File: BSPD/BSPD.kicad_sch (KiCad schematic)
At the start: 27 parts, among them J1 350826-1, J2 440054-2, Q3 PMOS, U1 LM339DR, U2 R-78E5.0-0.5, U3 SN74LVC1G08DBVR, U4 SN74LVC3G14DCUR, U5 NE555DR, U6 SN74LVC1G08DBVR, U7 SN74HC32DR

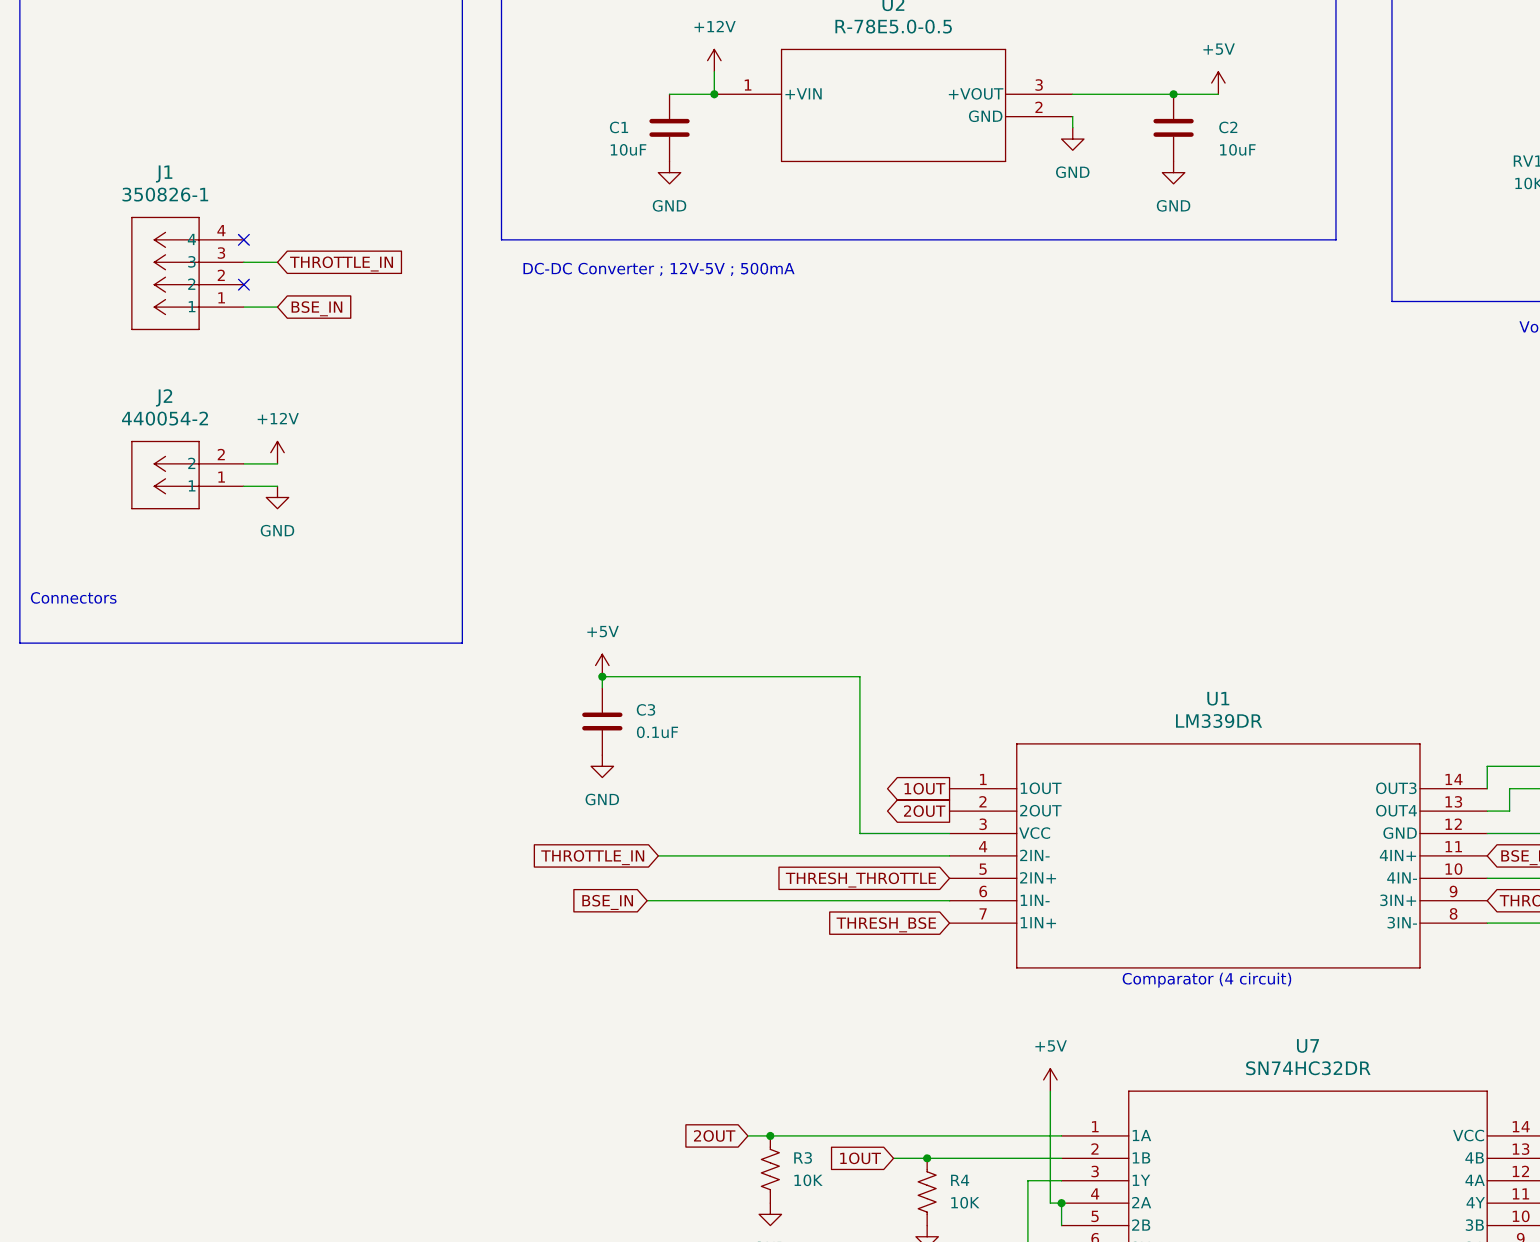
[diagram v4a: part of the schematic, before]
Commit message: Updating footprints
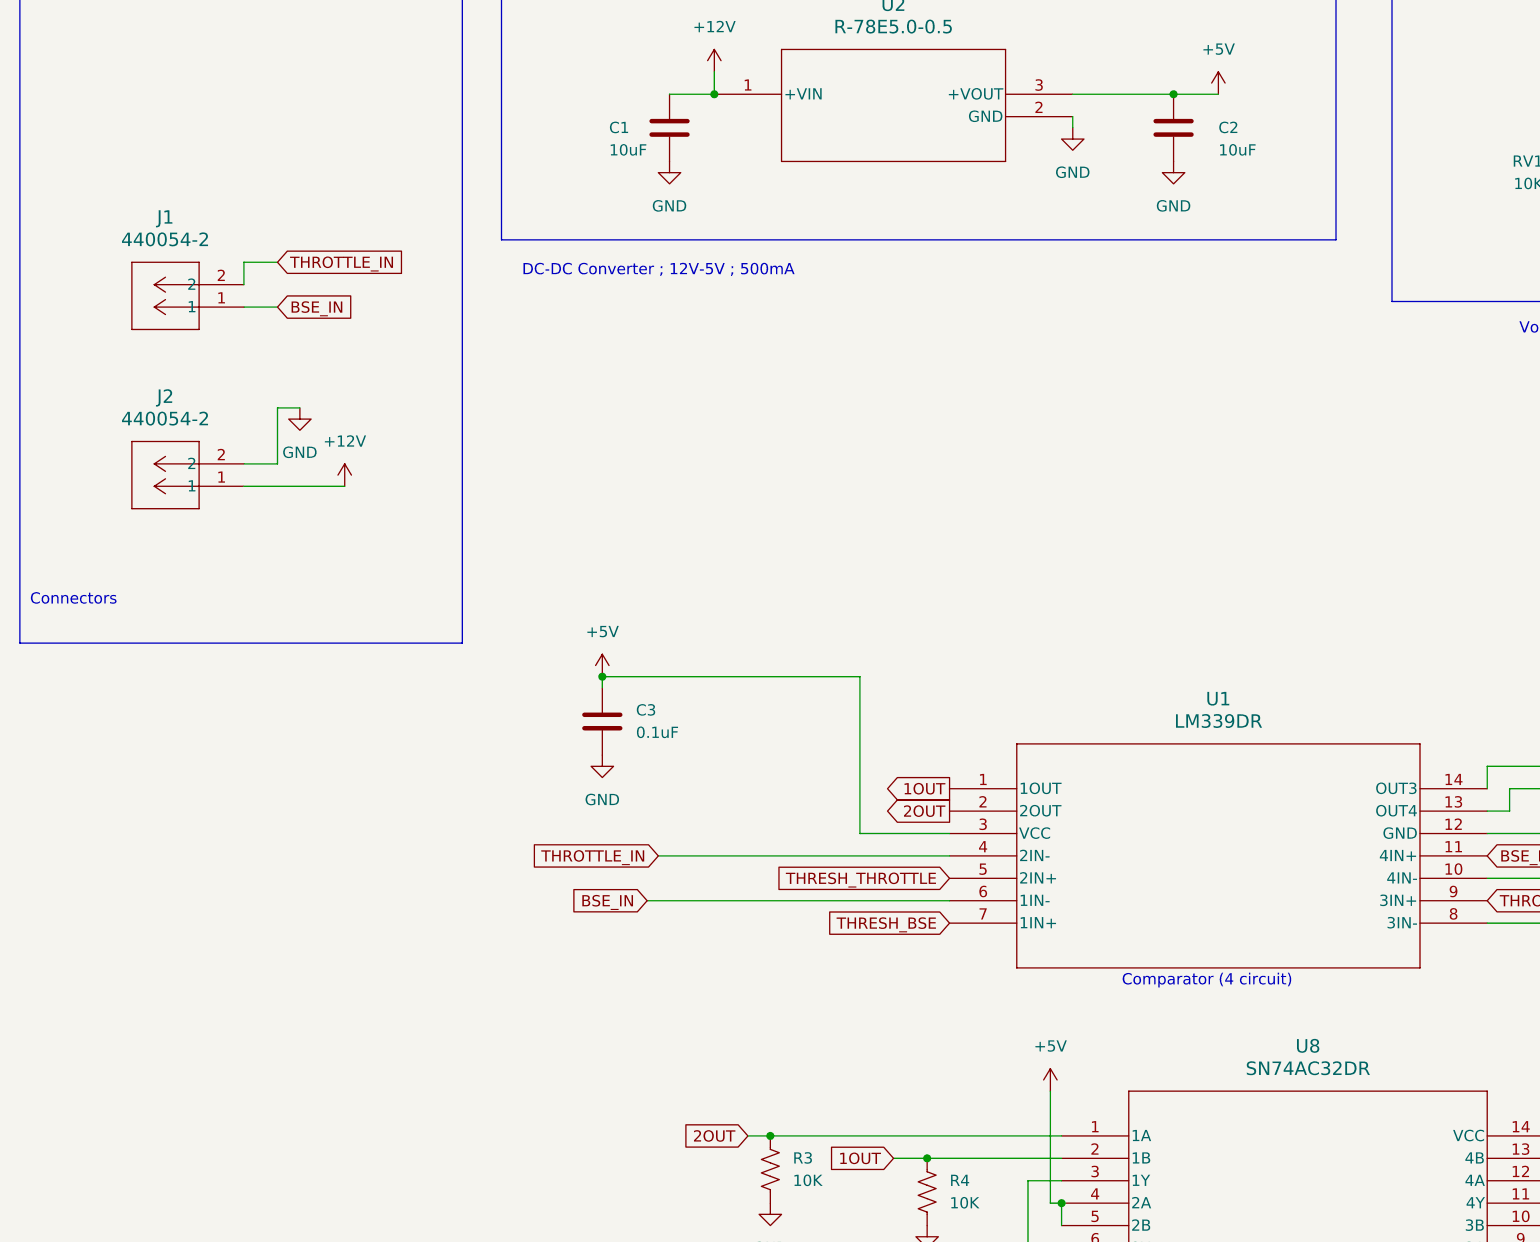
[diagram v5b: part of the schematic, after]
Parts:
- removed J1: 350826-1, 350826-1:CONN_350826-1_TYC, symbol 350826-1:350826-1
- removed U7: SN74HC32DR, SN74AC32DR:D14, symbol SN74AC32DR:SN74AC32DR
- added J1: 440054-2, 440054_2:CONN2_440054-2_TYC, symbol 440054_2:440054-2
- added U8: SN74AC32DR, D14, symbol SN74AC32DR:SN74AC32DR
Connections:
- net +12V: now also J2.1; no longer J2.2
- net 1OUT: now also U8.2 (1B)
- net 2OUT: now also U8.1 (1A)
- net BSE_IN: now also J1.1
- net BSPD_OUT: now also U8.8 (3Y)
- net GND: now also J2.2, U8.7 (GND); no longer J2.1
- net THROTTLE_IN: now also J1.2
- net at C7.1, R2.2: now also U8.10 (3B)
- net at C6.1: now also U8.12 (4A), U8.13 (4B), U8.14 (VCC)
- net at U4.1 (1A), U6.1 (A): now also U8.3 (1Y)
- net at U6.4 (Y): now also U8.9 (3A)
- new net: U8.4 (2A), U8.5 (2B)
- no-connect marks 2 -> 0

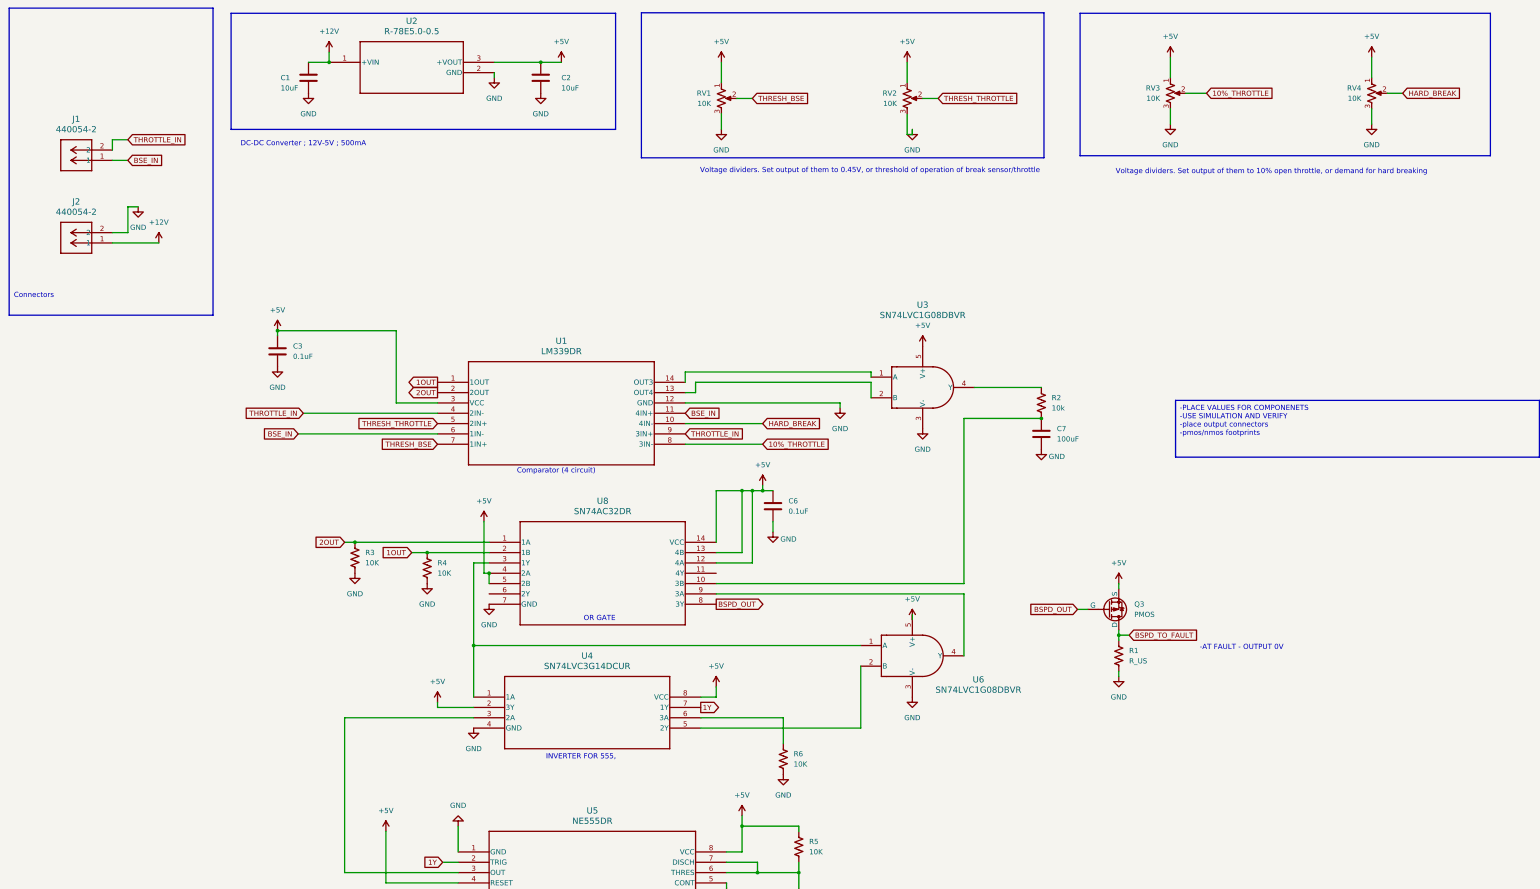
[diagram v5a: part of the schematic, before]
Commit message: Connector changes, layout, edge cuts, constraints. Need advice on output PMOS
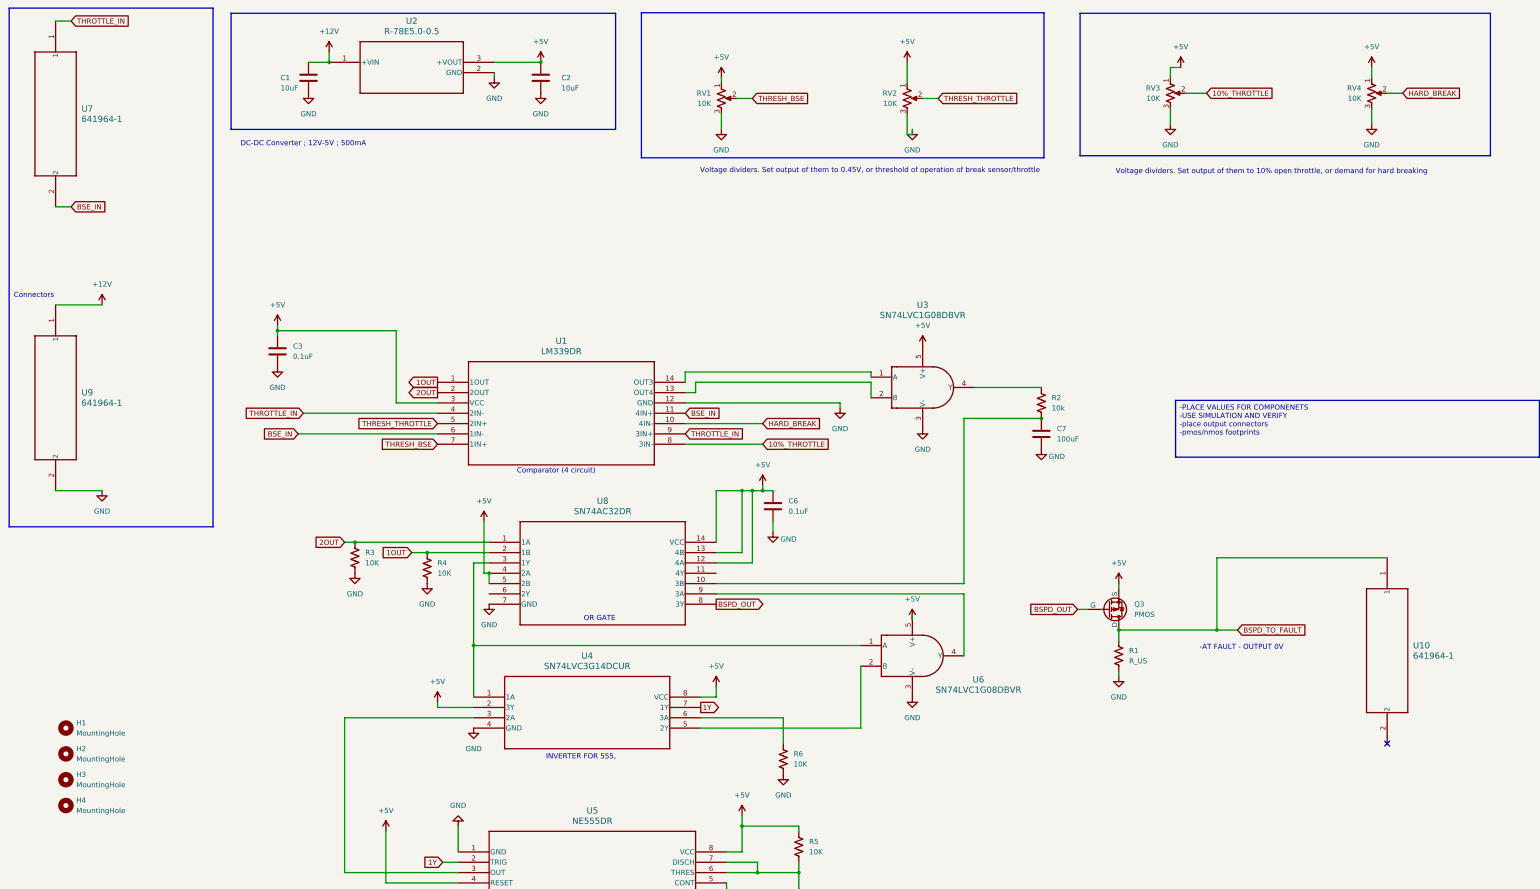
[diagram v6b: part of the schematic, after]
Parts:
- removed J1, J2: 440054-2, 440054_2:CONN2_440054-2_TYC, symbol 440054_2:440054-2
- added H1, H2, H3, H4: MountingHole, MountingHole:MountingHole_2.2mm_M2, symbol Mechanical:MountingHole
- added U10, U7, U9: 641964-1, 641964-1:641964-1_TYC, symbol 641964-1:641964-1
- Q3: footprint (none) -> Package_TO_SOT_SMD:SOT-23
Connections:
- net +12V: now also U9.1
- net +5V: now also C2.1, C3.1, RV1.1, RV2.1, RV3.1, RV4.1, U1.3 (VCC), U2.3 (+VOUT)
- net BSE_IN: now also U7.2
- net BSPD_TO_FAULT: now also U10.1
- net GND: now also U9.2
- net THROTTLE_IN: now also U7.1
- no-connect marks 0 -> 1

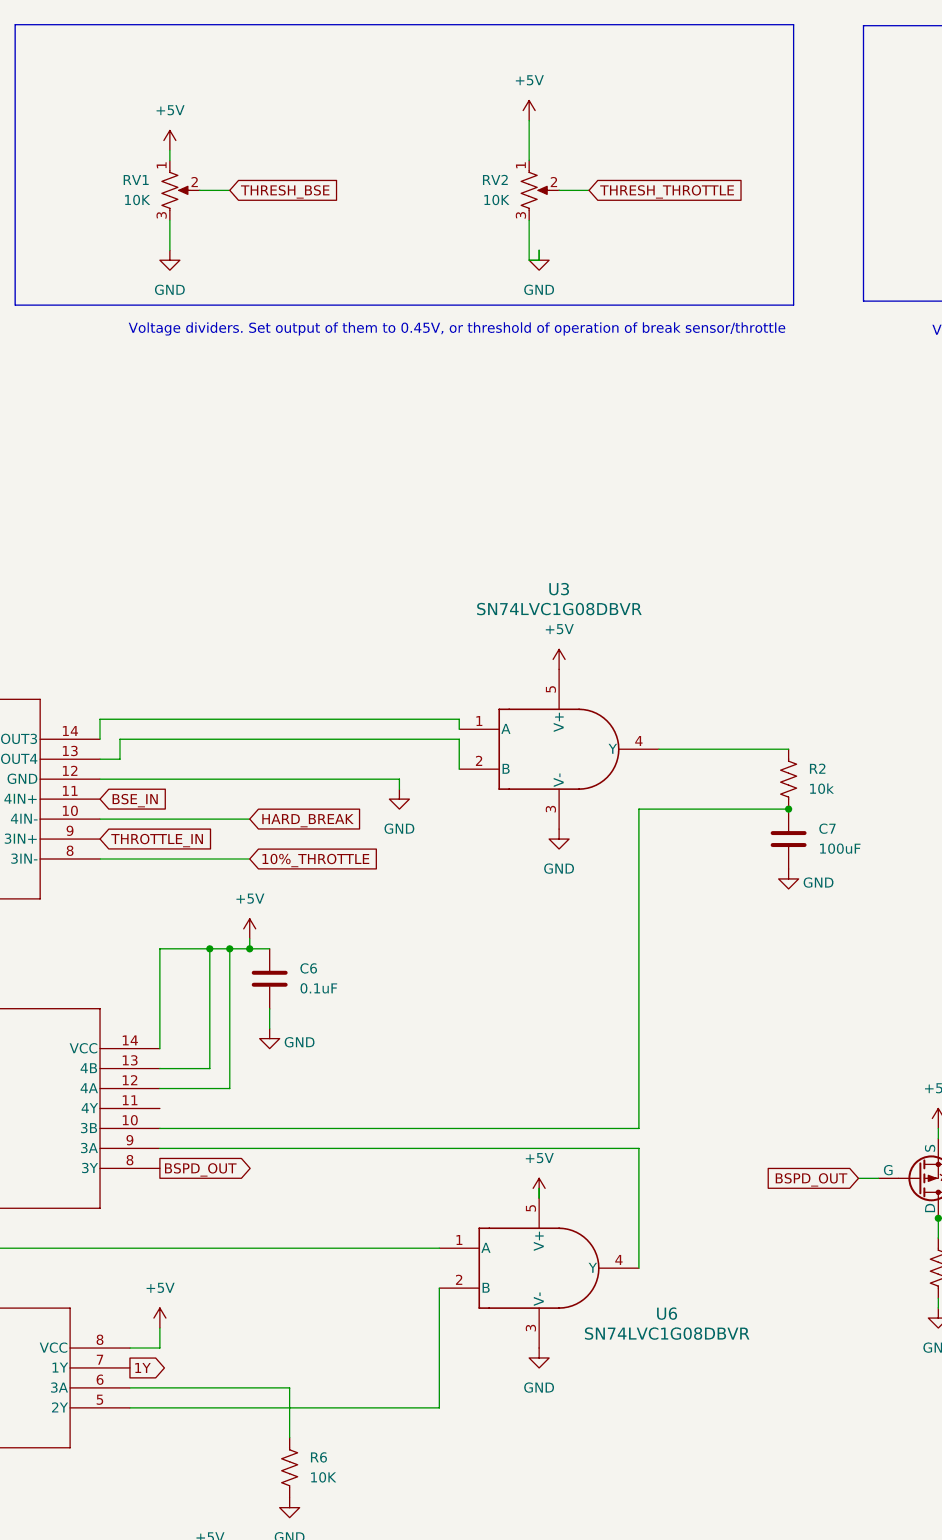
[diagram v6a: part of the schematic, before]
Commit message: Bypass caps bspd
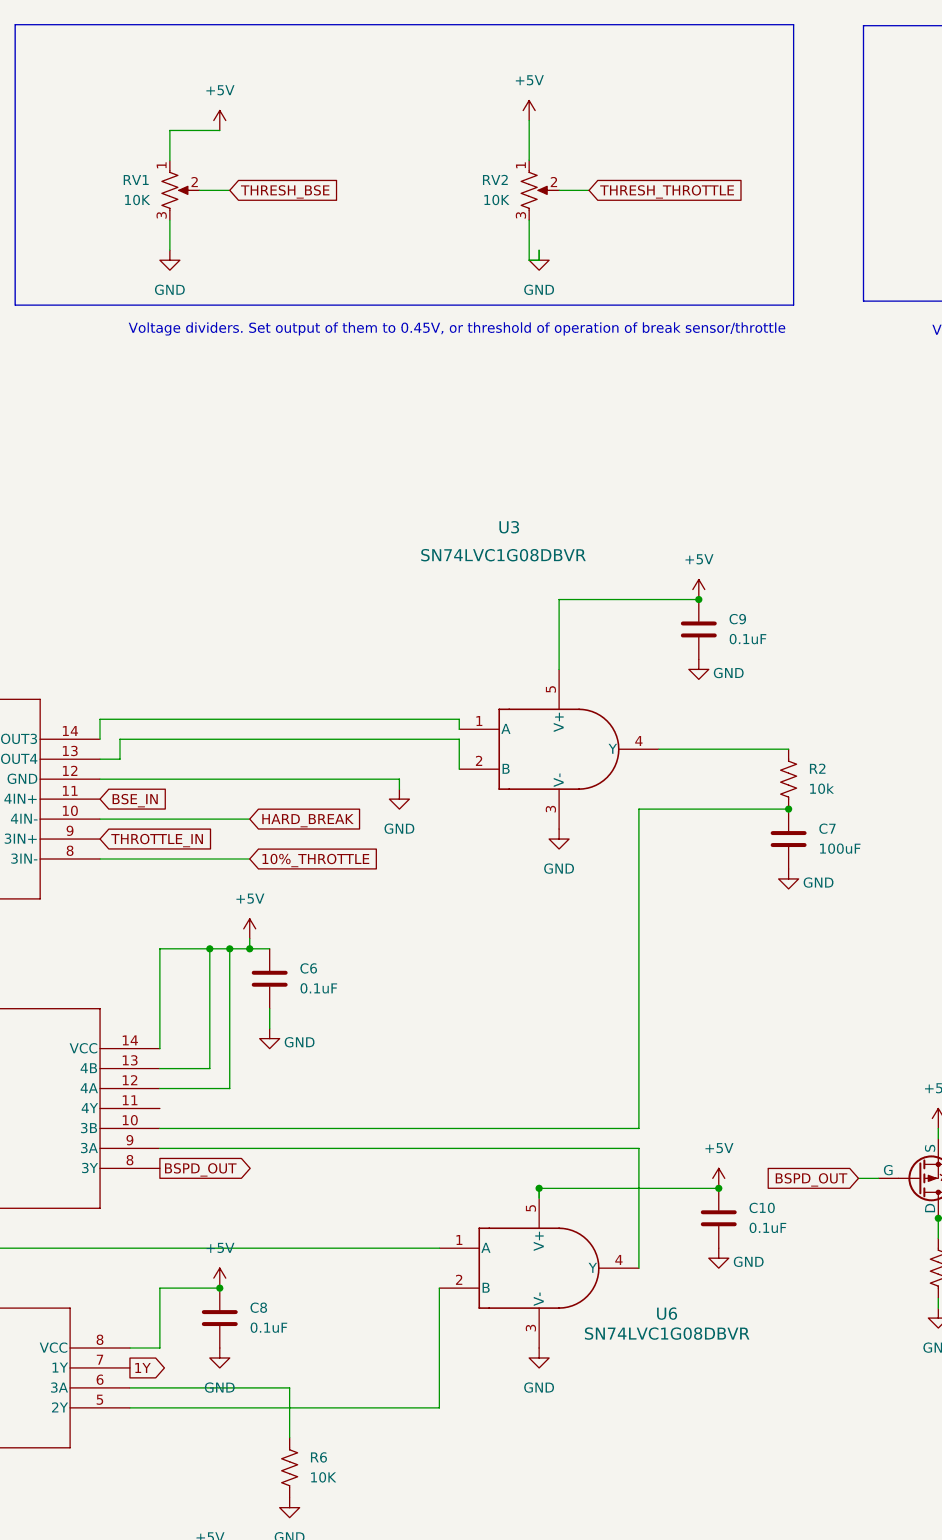
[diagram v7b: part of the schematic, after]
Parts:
- added C10, C8, C9: 0.1uF, Capacitor_SMD:C_0805_2012Metric, symbol Device:C
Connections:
- net +5V: now also C6.1, R5.2, U3.5 (V+), U4.2 (3Y), U4.8 (VCC), U5.4 (RESET), U5.8 (VCC), U6.5 (V+), U8.12 (4A), U8.13 (4B), U8.14 (VCC), U8.4 (2A), U8.5 (2B), C10.1, C8.1, C9.1
- net GND: now also C10.2, C8.2, C9.2
